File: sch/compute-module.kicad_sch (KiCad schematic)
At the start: 8 parts, among them J2 Conn_02x07_Odd_Even, J3 Conn_02x20_Odd_Even, SW1 SW_Push

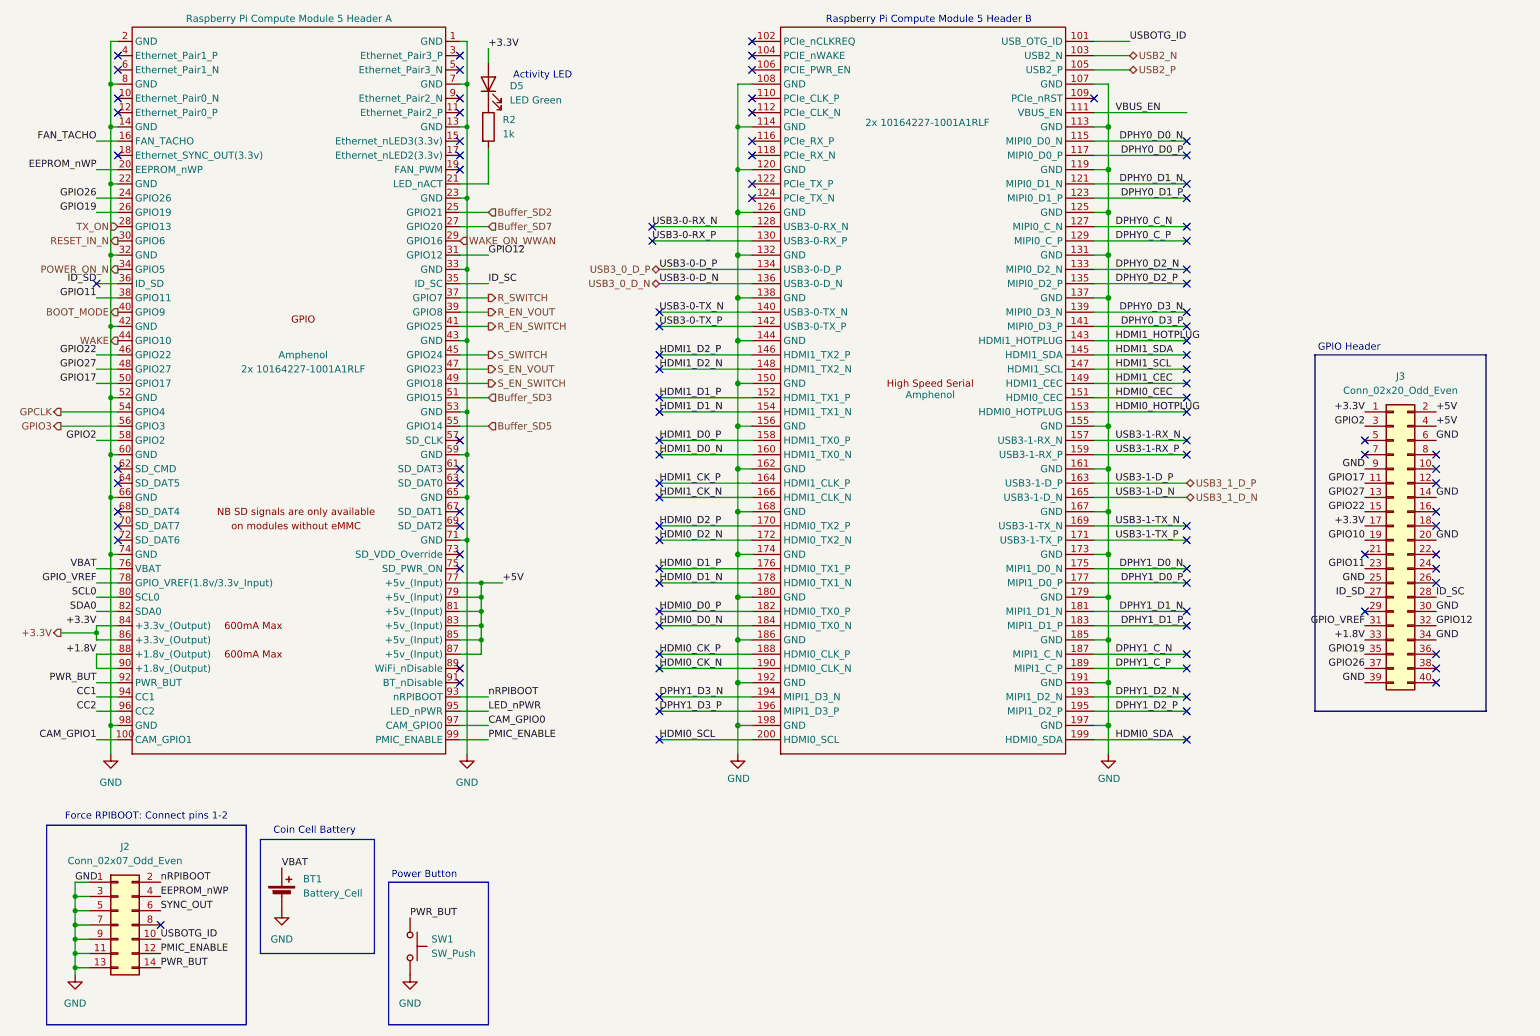
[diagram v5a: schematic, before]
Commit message: added more footprinst and esd
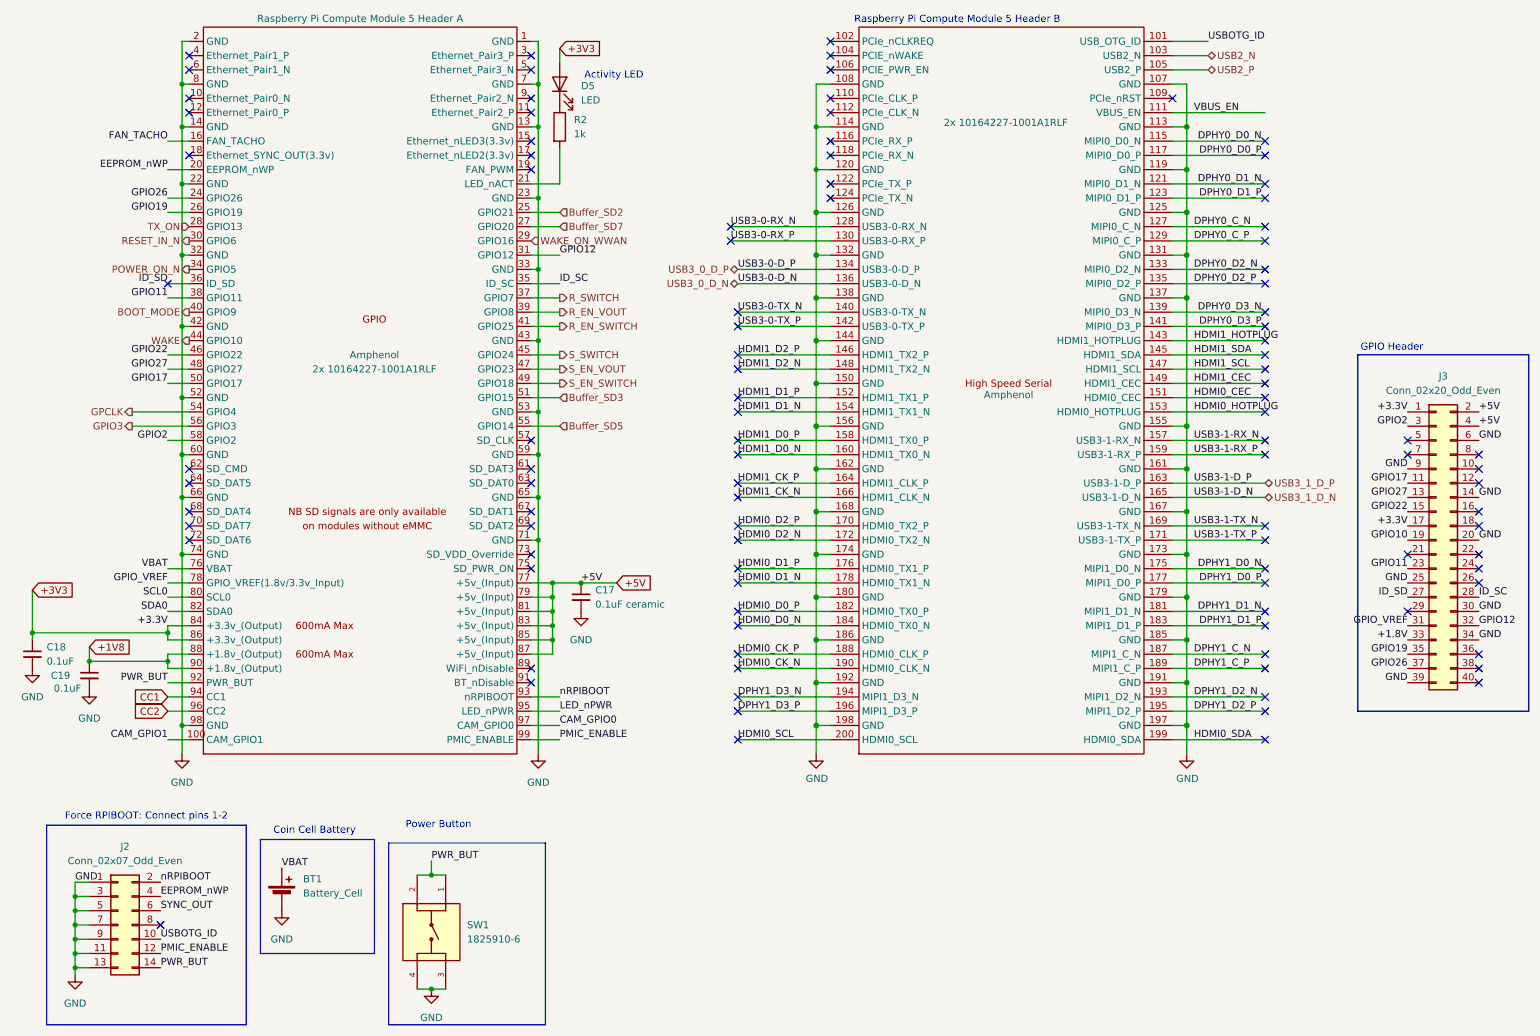
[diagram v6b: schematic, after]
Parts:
- removed SW1: SW_Push, symbol Switch:SW_Push
- added C17: 0.1uF ceramic, Capacitor_SMD:C_0603_1608Metric, symbol Device:C_Small
- added C18, C19: 0.1uF, Capacitor_SMD:C_0603_1608Metric, symbol Device:C_Small
- added SW1: 1825910-6, 1825910-6:SW_1825910-6-4, symbol 1825910-6:1825910-6
- BT1: footprint (none) -> Battery:BatteryHolder_Keystone_3034_1x20mm
- D5: value LED Green -> LED; footprint (none) -> LTST-C190GKT:LEDM1608X80; MPN (none) -> LTST-C190GKT
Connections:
- net +1.8V: no longer Module2.88 (+1.8v_(Output)), Module2.90 (+1.8v_(Output))
- net +5V: now also C17.1
- net GND: now also C17.2, C18.2, C19.2, SW1.3, SW1.4
- net PWR_BUT: now also SW1.1, SW1.2
- net +3.3V renamed +3V3
- net +3V3: now also C18.1
- new net +1V8: C19.1, Module2.88 (+1.8v_(Output)), Module2.90 (+1.8v_(Output))
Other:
- moved on the sheet: D5, J3, R2

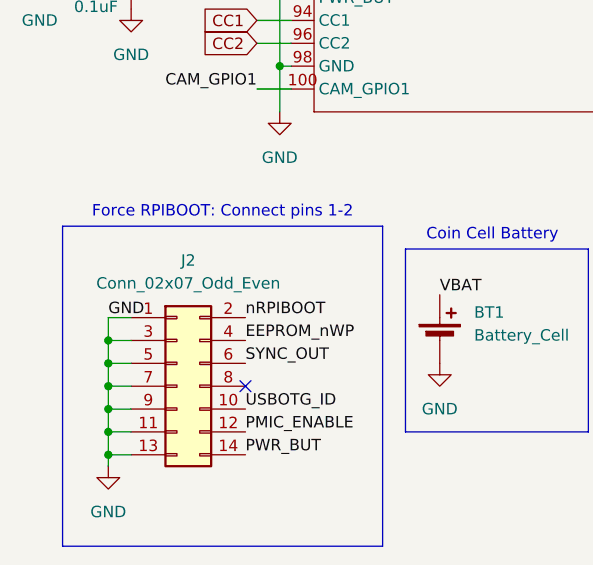
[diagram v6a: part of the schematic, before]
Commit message: added more footprints and added to pcb
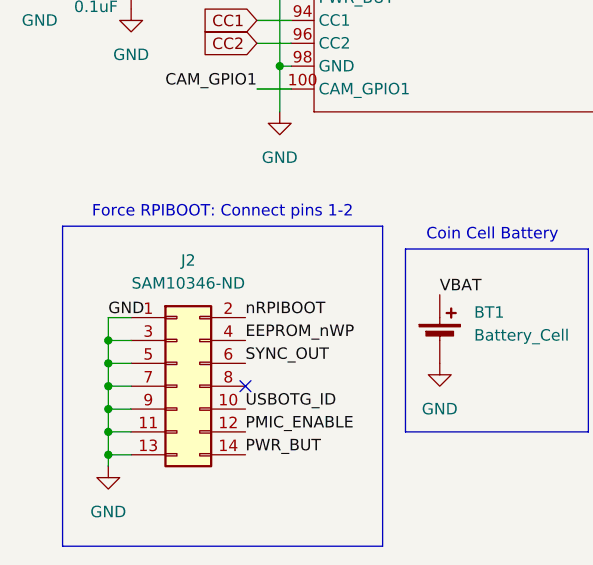
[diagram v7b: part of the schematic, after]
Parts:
- J2: value Conn_02x07_Odd_Even -> SAM10346-ND; footprint (none) -> Connector_PinSocket_2.54mm:PinSocket_2x07_P2.54mm_Vertical; MPN (none) -> SAM10346-ND
- J3: footprint (none) -> Connector_PinSocket_2.54mm:PinSocket_2x20_P2.54mm_Vertical; MPN (none) -> SAM10346-ND "KJØP TO!!!"
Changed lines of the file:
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@@
 			)
 		)
-		(property "Footprint" ""
+		(property "Footprint" "Connector_PinSocket_2.54mm:PinSocket_2x20_P2.54mm_Vertical"
 			(at 265.43 109.22 0)
 			(effects
@@
 		)
 		(property "Description" "Generic connector, double row, 02x20, odd/even pin numbering scheme (row 1 odd numbers, row 2 even numbers), script generated (kicad-library-utils/schlib/autogen/connector/)"
+			(at 265.43 109.22 0)
+			(effects
+				(font
+					(size 1.27 1.27)
+				)
+				(hide yes)
+			)
+		)
+		(property "MPN" "SAM10346-ND \"KJØP TO!!!\""
 			(at 265.43 109.22 0)
 			(effects
@@
 			)
 		)
-		(property "Value" "Conn_02x07_Odd_Even"
+		(property "Value" "SAM10346-ND"
 			(at 31.75 166.37 0)
 			(effects
@@
 			)
 		)
-		(property "Footprint" ""
+		(property "Footprint" "Connector_PinSocket_2.54mm:PinSocket_2x07_P2.54mm_Vertical"
 			(at 30.48 177.8 0)
 			(effects
@@
 			(at 30.48 177.8 0)
 			(effects
+				(font
+					(size 1.27 1.27)
+				)
+				(hide yes)
+			)
+		)
+		(property "MPN" "SAM10346-ND"
+			(at 30.48 177.8 0)
+			(effects

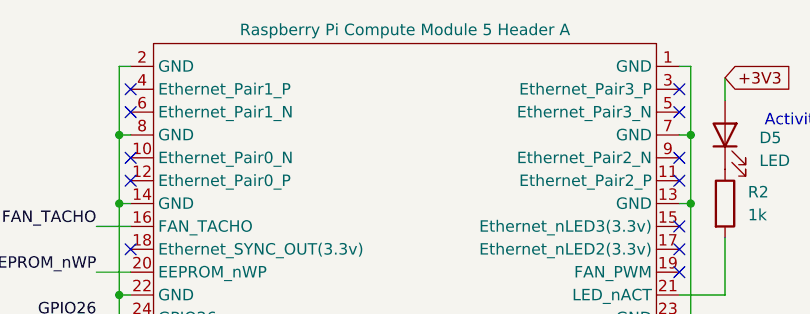
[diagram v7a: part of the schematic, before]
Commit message: added components
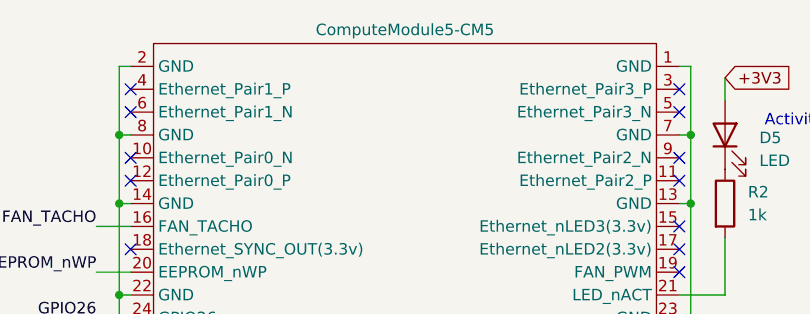
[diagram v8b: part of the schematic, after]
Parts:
- M1: renamed from Module2; value Raspberry Pi Compute Module 5 Header A -> ComputeModule5-CM5; footprint CM5IO:Raspberry-Pi-5-Compute-Module -> CM5108032:MODULE_CM5108032
- M1: renamed from Module1; footprint CM5IO:Raspberry-Pi-5-Compute-Module -> CM5108032:MODULE_CM5108032
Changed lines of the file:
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@@
 		(on_board yes)
 		(dnp no)
-		(property "Reference" "Module2"
+		(property "Reference" "M1"
 			(at 73.66 14.224 0)
 			(effects
@@
 			)
 		)
-		(property "Value" "Raspberry Pi Compute Module 5 Header A"
+		(property "Value" "ComputeModule5-CM5"
 			(at 73.66 16.256 0)
 			(effects
@@
 			)
 		)
-		(property "Footprint" "CM5IO:Raspberry-Pi-5-Compute-Module"
+		(property "Footprint" "CM5108032:MODULE_CM5108032"
 			(at 218.44 102.87 0)
 			(effects
@@
 			(project "audiograb"
 				(path "/c46c2311-6d4b-411d-b012-c7730eac136d/75b669f4-4784-4707-8d6c-b4da66be0510"
-					(reference "Module2")
+					(reference "M1")
 					(unit 1)
 				)
@@
 		(on_board yes)
 		(dnp no)
-		(property "Reference" "Module1"
+		(property "Reference" "M1"
 			(at 187.96 9.017 0)
 			(effects
@@
 			)
 		)
-		(property "Footprint" "CM5IO:Raspberry-Pi-5-Compute-Module"
+		(property "Footprint" "CM5108032:MODULE_CM5108032"
 			(at 190.5 107.95 0)
 			(effects
@@
 			(project "audiograb"
 				(path "/c46c2311-6d4b-411d-b012-c7730eac136d/75b669f4-4784-4707-8d6c-b4da66be0510"
-					(reference "Module1")
+					(reference "M1")
 					(unit 2)
 				)
